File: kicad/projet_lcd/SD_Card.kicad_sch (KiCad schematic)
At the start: 9 parts

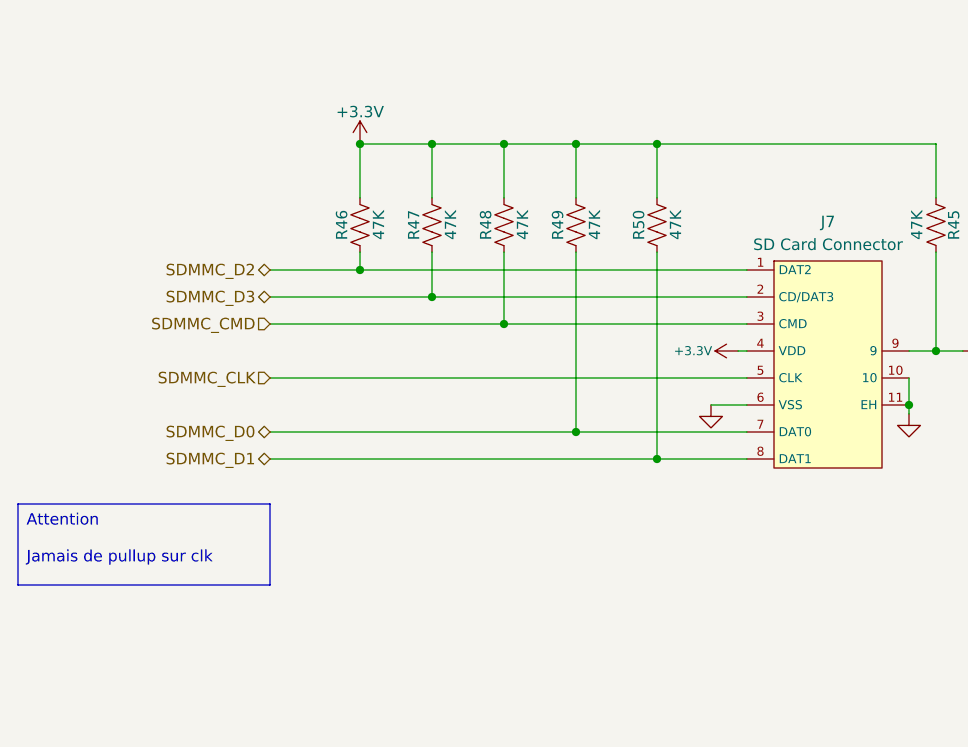
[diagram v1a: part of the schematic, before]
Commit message: cleaning up ERC alerts
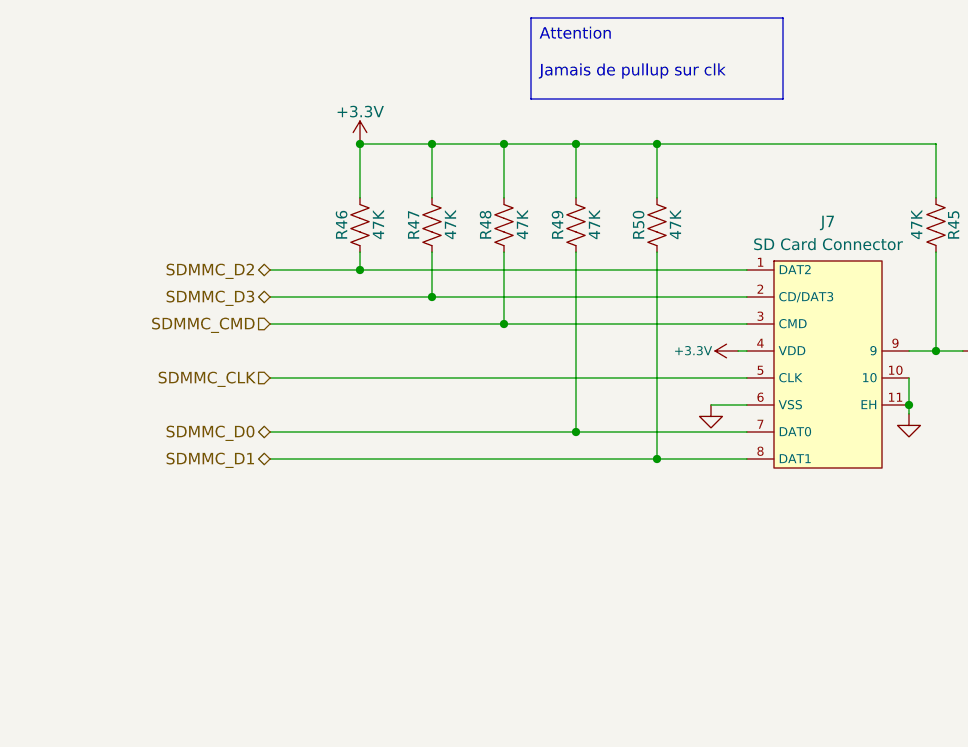
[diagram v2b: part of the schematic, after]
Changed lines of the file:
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@@
 	(text_box "Attention\n\nJamais de pullup sur clk"
 		(exclude_from_sim no)
-		(at 56 120 0)
+		(at 113 66 0)
 		(size 28 9)
 		(margins 0.9525 0.9525 0.9525 0.9525)
